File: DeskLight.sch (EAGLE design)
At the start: 39 parts, among them IC1 REG1117, J1 Würth Elektronik SD Connector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, T1 MMBT2222, T2 MMBT2222, T3 MJD122, T4 MJD122, T5 MJD122, U1 ESP32-WROOM-32D, U2 CH340C

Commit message: .
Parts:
- IC1: device burr-brown:REG1117 -> burr-brown_:REG1117
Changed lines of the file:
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@@
 </classes>
 <parts>
-<part name="J1" library="693071030811_Eagle_WR-CRD_rev20b" deviceset="693071020811" device="" package3d_urn="urn:adsk.eagle:package:16444883/2" value="Würth Elektronik SD Connector 693071020811"/>
-<part name="IC1" library="burr-brown" library_urn="urn:adsk.eagle:library:111" deviceset="REG1117" device="" package3d_urn="urn:adsk.eagle:package:4940/1"/>
+<part name="J1" library="693071030811_Eagle_WR-CRD_rev20b" deviceset="693071020811" device="" package3d_urn="urn:adsk.eagle:package:16444883/2" override_package3d_urn="urn:adsk.eagle:package:21154478/3" override_package_urn="urn:adsk.eagle:footprint:16444854/1" value="Würth Elektronik SD Connector 693071020811"/>
+<part name="IC1" library="burr-brown_" deviceset="REG1117" device="" package3d_urn="urn:adsk.eagle:package:21174474/2"/>
 <part name="C1" library="rcl" library_urn="urn:adsk.eagle:library:334" deviceset="CPOL-EU" device="CT3216" package3d_urn="urn:adsk.eagle:package:23327/2" value="22uF"/>
 <part name="GND1" library="supply1" library_urn="urn:adsk.eagle:library:371" deviceset="GND" device=""/>
@@
 <part name="R3" library="rcl" library_urn="urn:adsk.eagle:library:334" deviceset="R-US_" device="R0603" package3d_urn="urn:adsk.eagle:package:23555/3" value="10k"/>
 <part name="GND2" library="supply1" library_urn="urn:adsk.eagle:library:371" deviceset="GND" device=""/>
-<part name="U1" library="ESP32-WROOM-32D" deviceset="ESP32-WROOM-32D" device=""/>
+<part name="U1" library="ESP32-WROOM-32D" library_urn="urn:adsk.eagle:library:21173998" deviceset="ESP32-WROOM-32D" device="" package3d_urn="urn:adsk.eagle:package:21174001/2"/>
 <part name="T1" library="transistor" library_urn="urn:adsk.eagle:library:402" deviceset="*-NPN-" device="SOT23-BEC" package3d_urn="urn:adsk.eagle:package:28748/2" technology="MMBT2222ALT1" value="MMBT2222"/>
 <part name="T2" library="transistor" library_urn="urn:adsk.eagle:library:402" deviceset="*-NPN-" device="SOT23-BEC" package3d_urn="urn:adsk.eagle:package:28748/2" technology="MMBT2222ALT1" value="MMBT2222"/>
@@
 <part name="C3" library="rcl" library_urn="urn:adsk.eagle:library:334" deviceset="C-EU" device="C0603K" package3d_urn="urn:adsk.eagle:package:23680/2" value="1uF"/>
 <part name="GND3" library="supply1" library_urn="urn:adsk.eagle:library:371" deviceset="GND" device=""/>
-<part name="RESET" library="adafruit" library_urn="urn:adsk.eagle:library:420" deviceset="SPST_TACT" device="-KMR2" package3d_urn="urn:adsk.eagle:package:6240885/1" value="KMR2"/>
+<part name="RESET" library="adafruit" library_urn="urn:adsk.eagle:library:21174610" deviceset="SPST_TACT" device="-KMR2" package3d_urn="urn:adsk.eagle:package:21174604/2" override_package3d_urn="urn:adsk.eagle:package:21154607/4" override_package_urn="urn:adsk.eagle:footprint:6240242/1" value="KMR2"/>
 <part name="GND4" library="supply1" library_urn="urn:adsk.eagle:library:371" deviceset="GND" device=""/>
-<part name="BOOT" library="adafruit" library_urn="urn:adsk.eagle:library:420" deviceset="SPST_TACT" device="-KMR2" package3d_urn="urn:adsk.eagle:package:6240885/1" value="KMR2"/>
+<part name="BOOT" library="adafruit" library_urn="urn:adsk.eagle:library:21174610" deviceset="SPST_TACT" device="-KMR2" package3d_urn="urn:adsk.eagle:package:21174604/2" override_package3d_urn="urn:adsk.eagle:package:21174067/2" override_package_urn="urn:adsk.eagle:footprint:6240242/1" value="KMR2"/>
 <part name="GND16" library="supply1" library_urn="urn:adsk.eagle:library:371" deviceset="GND" device=""/>
 <part name="+3V2" library="supply1" library_urn="urn:adsk.eagle:library:371" deviceset="+3V3" device=""/>
 <part name="GND5" library="supply1" library_urn="urn:adsk.eagle:library:371" deviceset="GND" device=""/>
-<part name="U2" library="SparkFun-IC-Comms" deviceset="CH340C" device=""/>
+<part name="U2" library="SparkFun-IC-Comms" library_urn="urn:adsk.eagle:library:21174484" deviceset="CH340C" device="" package3d_urn="urn:adsk.eagle:package:21174539/2"/>
 <part name="RX" library="led" library_urn="urn:adsk.eagle:library:259" deviceset="LED" device="CHIP-LED0603" package3d_urn="urn:adsk.eagle:package:15819/3" value="BLUE"/>
 <part name="TX" library="led" library_urn="urn:adsk.eagle:library:259" deviceset="LED" device="CHIP-LED0603" package3d_urn="urn:adsk.eagle:package:15819/3" value="RED"/>
@@
 <part name="C5" library="rcl" library_urn="urn:adsk.eagle:library:334" deviceset="C-EU" device="C0603K" package3d_urn="urn:adsk.eagle:package:23680/2" value="0.1uF"/>
 <part name="GND11" library="supply1" library_urn="urn:adsk.eagle:library:371" deviceset="GND" device=""/>
-<part name="USB" library="con-molex-usb" deviceset="MICRO-USB-RECEPTACLE" device="47589-0001" value="MICRO-USB-47589-0001"/>
+<part name="USB" library="con-molex-usb" library_urn="urn:adsk.eagle:library:21174025" deviceset="MICRO-USB-RECEPTACLE" device="47589-0001" package3d_urn="urn:adsk.eagle:package:21174028/2" value="MICRO-USB-47589-0001"/>
 <part name="C4" library="rcl" library_urn="urn:adsk.eagle:library:334" deviceset="C-EU" device="C0603K" package3d_urn="urn:adsk.eagle:package:23680/2" value="0.1uF"/>
 <part name="GND6" library="supply1" library_urn="urn:adsk.eagle:library:371" deviceset="GND" device=""/>
@@
 <part name="GND15" library="supply1" library_urn="urn:adsk.eagle:library:371" deviceset="GND" device=""/>
 <part name="+3V11" library="supply1" library_urn="urn:adsk.eagle:library:371" deviceset="+3V3" device=""/>
-<part name="+12V" library="wirepad" library_urn="urn:adsk.eagle:library:412" deviceset="WIREPAD" device="SMD5-1,8" package3d_urn="urn:adsk.eagle:package:30844/1" value="LEDPAD"/>
-<part name="GREEN" library="wirepad" library_urn="urn:adsk.eagle:library:412" deviceset="WIREPAD" device="SMD5-1,8" package3d_urn="urn:adsk.eagle:package:30844/1" value="LEDPAD"/>
-<part name="RED" library="wirepad" library_urn="urn:adsk.eagle:library:412" deviceset="WIREPAD" device="SMD5-1,8" package3d_urn="urn:adsk.eagle:package:30844/1" value="LEDPAP"/>
-<part name="BLUE" library="wirepad" library_urn="urn:adsk.eagle:library:412" deviceset="WIREPAD" device="SMD5-1,8" package3d_urn="urn:adsk.eagle:package:30844/1" value="LEDPAD"/>
-<part name="VIN" library="wirepad" library_urn="urn:adsk.eagle:library:412" deviceset="WIREPAD" device="SMD5-1,8" package3d_urn="urn:adsk.eagle:package:30844/1" value="LEDPAD"/>
-<part name="GND" library="wirepad" library_urn="urn:adsk.eagle:library:412" deviceset="WIREPAD" device="SMD5-1,8" package3d_urn="urn:adsk.eagle:package:30844/1" value="LEDPAD"/>
-<part name="T3" library="transistor-neu-to92" library_urn="urn:adsk.eagle:library:397" deviceset="MJD31*" device="" package3d_urn="urn:adsk.eagle:package:28765/2" value="MJD122"/>
-<part name="T4" library="transistor-neu-to92" library_urn="urn:adsk.eagle:library:397" deviceset="MJD31*" device="" package3d_urn="urn:adsk.eagle:package:28765/2" value="MJD122"/>
-<part name="T5" library="transistor-neu-to92" library_urn="urn:adsk.eagle:library:397" deviceset="MJD31*" device="" package3d_urn="urn:adsk.eagle:package:28765/2" value="MJD122"/>
+<part name="+12V" library="wirepad" library_urn="urn:adsk.eagle:library:21175076" deviceset="WIREPAD" device="SMD5-1,8" package3d_urn="urn:adsk.eagle:package:21175074/2" value="LEDPAD"/>
+<part name="GREEN" library="wirepad" library_urn="urn:adsk.eagle:library:21175076" deviceset="WIREPAD" device="SMD5-1,8" package3d_urn="urn:adsk.eagle:package:21175074/2" value="LEDPAD"/>
+<part name="RED" library="wirepad" library_urn="urn:adsk.eagle:library:21175076" deviceset="WIREPAD" device="SMD5-1,8" package3d_urn="urn:adsk.eagle:package:21175074/2" value="LEDPAP"/>
+<part name="BLUE" library="wirepad" library_urn="urn:adsk.eagle:library:21175076" deviceset="WIREPAD" device="SMD5-1,8" package3d_urn="urn:adsk.eagle:package:21175074/2" value="LEDPAD"/>
+<part name="VIN" library="wirepad" library_urn="urn:adsk.eagle:library:21175076" deviceset="WIREPAD" device="SMD5-1,8" package3d_urn="urn:adsk.eagle:package:21175074/2" value="LEDPAD"/>
+<part name="GND" library="wirepad" library_urn="urn:adsk.eagle:library:21175076" deviceset="WIREPAD" device="SMD5-1,8" package3d_urn="urn:adsk.eagle:package:21175074/2" value="LEDPAD"/>
+<part name="T3" library="transistor-neu-to92" library_urn="urn:adsk.eagle:library:397" deviceset="MJD31*" device="" package3d_urn="urn:adsk.eagle:package:28765/2" override_package3d_urn="urn:adsk.eagle:package:21154560/2" override_package_urn="urn:adsk.eagle:footprint:28703/1" value="MJD122"/>
+<part name="T4" library="transistor-neu-to92" library_urn="urn:adsk.eagle:library:397" deviceset="MJD31*" device="" package3d_urn="urn:adsk.eagle:package:28765/2" override_package3d_urn="urn:adsk.eagle:package:21154548/2" override_package_urn="urn:adsk.eagle:footprint:28703/1" value="MJD122"/>
+<part name="T5" library="transistor-neu-to92" library_urn="urn:adsk.eagle:library:397" deviceset="MJD31*" device="" package3d_urn="urn:adsk.eagle:package:28765/2" override_package3d_urn="urn:adsk.eagle:package:21154542/2" override_package_urn="urn:adsk.eagle:footprint:28703/1" value="MJD122"/>
 <part name="+3V12" library="supply1" library_urn="urn:adsk.eagle:library:371" deviceset="+3V3" device=""/>
 <part name="R11" library="rcl" library_urn="urn:adsk.eagle:library:334" deviceset="R-US_" device="R0603" package3d_urn="urn:adsk.eagle:package:23555/3" value="1k"/>
@@
 packages will not be understood (or retained) with this version.
 </note>
+<note version="9.4" severity="warning">
+Since Version 9.4, EAGLE supports the overriding of 3D packages
+in schematics and board files. Those overridden 3d packages
+will not be understood (or retained) with this version.
+</note>
 <note version="8.4" severity="warning">

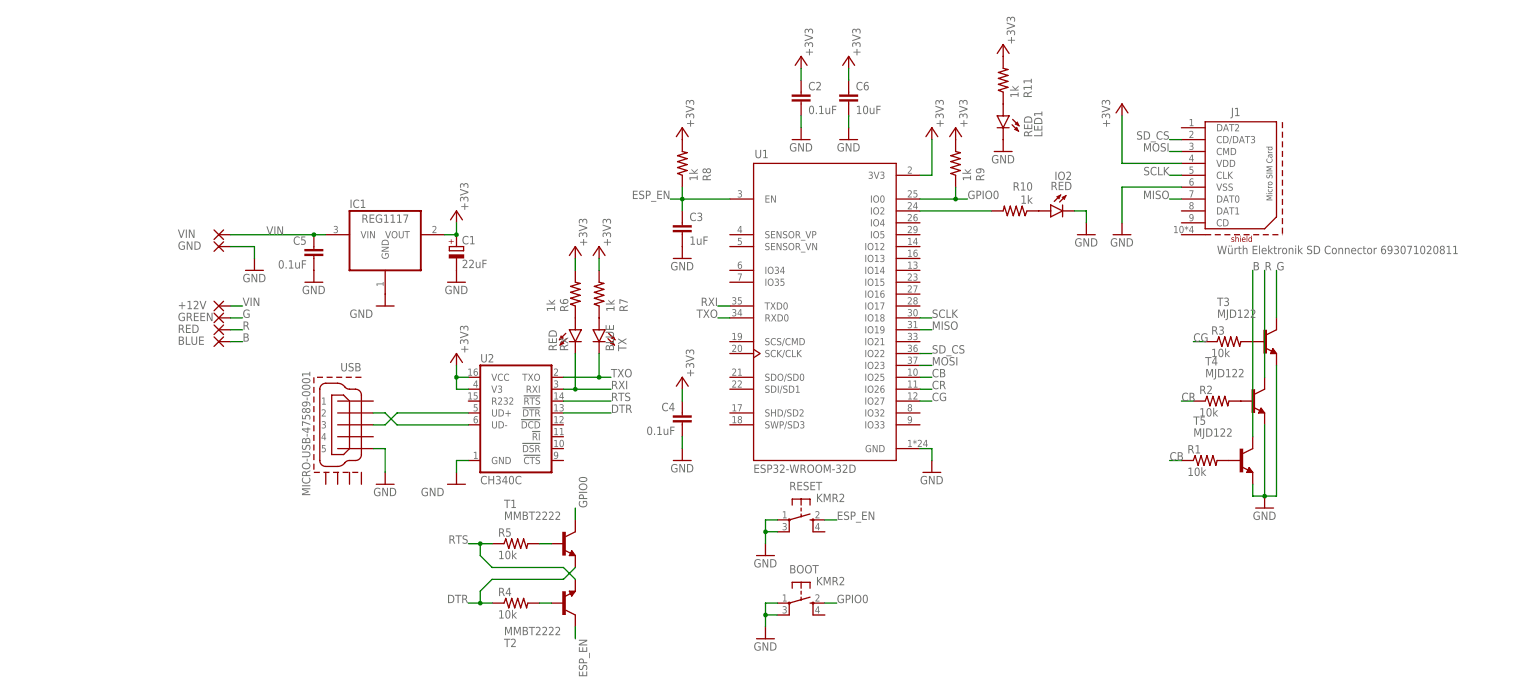
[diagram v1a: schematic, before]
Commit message: new version with small size and for addressable led strips
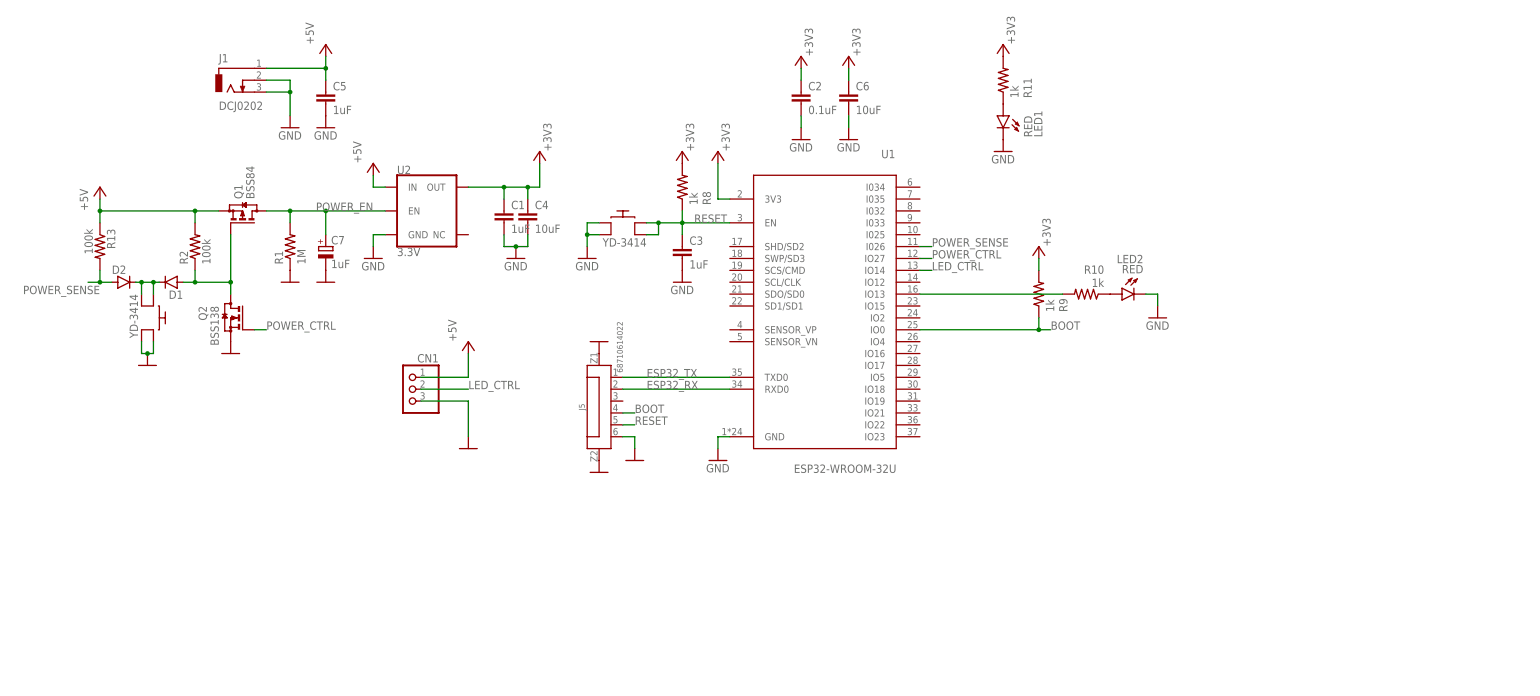
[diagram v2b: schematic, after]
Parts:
- removed +12V, BLUE, GND, GREEN, VIN: LEDPAD, wirepad:WIREPADSMD5-1,8
- removed BOOT, RESET: KMR2, adafruit:SPST_TACT-KMR2
- removed IC1: REG1117, burr-brown_:REG1117
- removed IO2, TX: RED, led:LEDCHIP-LED0603
- removed R3, R4, R5: 10k, rcl:R-US_R0603
- removed R6, R7: 1k, rcl:R-US_R0603
- removed RED: LEDPAP, wirepad:WIREPADSMD5-1,8
- removed RX: BLUE, led:LEDCHIP-LED0603
- removed T1, T2: MMBT2222, transistor:MMBT2222ALT1-NPN-SOT23-BEC
- removed T3, T4, T5: MJD122, transistor-neu-to92:MJD31
- removed USB: MICRO-USB-47589-0001, con-molex-usb:MICRO-USB-RECEPTACLE47589-0001
- added C7: 1uF, rcl:CPOL-EUCT3216
- added CN1: (no value), adafruit:JST_3PIN
- added D1, D2: (no value), semicon-smd-ipc:D-SOD123
- added J5: 68710614022, WR-FPC:6871XX14022_68710614022
- added LED2: RED, led:LEDMICRO-SIDELED
- added Q1: BSS84, transistor-small-signal:BSS84
- added Q2: BSS138, transistor-small-signal:BSS123
- added R13: 100k, rcl:R-US_R0603
- added U$1, U$67: YD-3414, YD-3414:YD-3414
- C1: value 22uF -> 1uF; device rcl:CPOL-EUCT3216 -> rcl:C-EUC0603K
- C4: value 0.1uF -> 10uF; device rcl:C-EUC0603K -> rcl:C-EUC0805
- C5: value 0.1uF -> 1uF
- C6: device rcl:C-EUC0603K -> rcl:C-EUC0805
- J1: value Würth Elektronik SD Connector 693071020811 -> DCJ0202; device 693071030811_Eagle_WR-CRD_rev20b:693071020811 -> con-jack:DCJ0202
- LED1: device led:LEDCHIP-LED0603 -> led:LEDMICRO-SIDELED
- R1: value 10k -> 1M
- R2: value 10k -> 100k
- U1: value ESP32-WROOM-32D -> ESP32-WROOM-32U; device ESP32-WROOM-32D:ESP32-WROOM-32D -> ESP32-WROOM-32U:ESP32-WROOM-32U
- U2: value CH340C -> 3.3V; device SparkFun-IC-Comms:CH340C -> SparkFun-IC-Power:V_REG_AP2112K-3.3V
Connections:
- removed net B: BLUE.P, T5.C
- removed net CB: R1.1, U1.IO25
- removed net CG: R3.1, U1.IO27
- removed net CR: R2.1, U1.IO26
- removed net DTR: R4.1, T1.E, U2.!DTR
- removed net ESP_EN: C3.1, R8.1, RESET.S, T2.C, U1.EN
- removed net G: GREEN.P, T3.C
- removed net GPIO0: BOOT.S, R9.1, T1.C, U1.IO0
- removed net MISO: J1.DAT0, U1.IO19
- removed net MOSI: J1.CMD, U1.IO23
- removed net N$10: R10.2, U1.IO2
- removed net N$12: U2.UD-, USB.2
- removed net N$3: R5.2, T1.B
- removed net N$4: R4.2, T2.B
- removed net N$5: R6.1, RX.A
- removed net N$6: R7.1, TX.A
- removed net N$7: R3.2, T3.B
- removed net R: RED.P, T4.C
- removed net RTS: R5.1, T2.E, U2.!RTS
- removed net RXI: RX.C, U1.TXD0, U2.RXI
- removed net SCLK: J1.CLK, U1.IO18
- removed net SD_CS: J1.CD/DAT3, U1.IO22
- removed net TXO: TX.C, U1.RXD0, U2.TXO
- removed net VIN: +12V.P, C5.1, IC1.VIN, VIN.P
- new net +5V: C5.1, CN1.1, J1.1, Q1.S, R13.1, R2.2, U2.IN
- new net BOOT: J5.4, R9.1, U1.IO0
- new net ESP32_RX: J5.2, U1.RXD0
- new net ESP32_TX: J5.1, U1.TXD0
- new net LED_CTRL: CN1.2, U1.IO14
- new net POWER_CTRL: Q2.G, U1.IO27
- new net POWER_EN: C7.+, Q1.D, R1.2, U2.EN
- new net POWER_SENSE: D2.A, R13.2, U1.I026
- new net RESET: C3.1, J5.5, R8.1, U$1.P$1, U$1.P$2, U1.EN
- net +3V3: now also C1.1, U2.OUT; no longer C1.+, IC1.VOUT, J1.VDD, R6.2, R7.2, U2.V3, U2.VCC
- net GND: now also C1.2, C7.-, CN1.3, J1.2, J1.3, J5.6, J5.Z1, J5.Z2, LED2.C, Q2.S, R1.1, U$1.P$3, U$1.P$4, U$67.P$3, U$67.P$4; no longer BOOT.P, BOOT.P1, C1.-, GND.P, IC1.GND, IO2.C, J1.VSS, RESET.P, RESET.P1, T3.E, T4.E, T5.E, USB.5
- net N$1: now also D1.A, Q1.G, Q2.D, R2.1; no longer R1.2, T5.B
- net N$11: now also D1.C, D2.C, U$67.P$1, U$67.P$2; no longer U2.UD+, USB.3
- net N$13: now also LED2.A; no longer IO2.A
- net N$2: now also R10.2, U1.IO13; no longer R2.2, T4.B
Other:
- moved on the sheet: C3, C4, C5, R1, R10, R2, R8, R9

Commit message: reviewed
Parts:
- C1, C2, C3, C5: device rcl:C-EUC0603K -> rcl:C-EUC0603
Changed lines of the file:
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@@
 <?xml version="1.0" encoding="utf-8"?>
 <!DOCTYPE eagle SYSTEM "eagle.dtd">
-<eagle version="9.6.2">
+<eagle version="9.4.0">
 <drawing>
 <settings>
-<setting alwaysvectorfont="yes"/>
+<setting alwaysvectorfont="no"/>
 <setting verticaltext="up"/>
 </settings>
@@
 <parts>
 <part name="GND2" library="supply1" library_urn="urn:adsk.eagle:library:371" deviceset="GND" device=""/>
-<part name="U1" library="ESP32-WROOM-32U" deviceset="ESP32-WROOM-32U" device="" override_package3d_urn="urn:adsk.eagle:package:27501419/2" override_package_urn="urn:adsk.eagle:footprint:27501420/1"/>
-<part name="C3" library="rcl" library_urn="urn:adsk.eagle:library:334" deviceset="C-EU" device="C0603K" package3d_urn="urn:adsk.eagle:package:23680/2" value="1uF"/>
+<part name="U1" library="ESP32-WROOM-32U" deviceset="ESP32-WROOM-32U" device="" override_package3d_urn="urn:adsk.eagle:package:27501419/2" override_package_urn="urn:adsk.eagle:footprint:27501420/1" override_locally_modified="yes"/>
+<part name="C3" library="rcl" library_urn="urn:adsk.eagle:library:334" deviceset="C-EU" device="C0603" package3d_urn="urn:adsk.eagle:package:23616/2" value="1uF"/>
 <part name="GND3" library="supply1" library_urn="urn:adsk.eagle:library:371" deviceset="GND" device=""/>
 <part name="GND4" library="supply1" library_urn="urn:adsk.eagle:library:371" deviceset="GND" device=""/>
@@
 <part name="+3V7" library="supply1" library_urn="urn:adsk.eagle:library:371" deviceset="+3V3" device=""/>
 <part name="+3V1" library="supply1" library_urn="urn:adsk.eagle:library:371" deviceset="+3V3" device=""/>
-<part name="C2" library="rcl" library_urn="urn:adsk.eagle:library:334" deviceset="C-EU" device="C0603K" package3d_urn="urn:adsk.eagle:package:23680/2" value="0.1uF"/>
+<part name="C2" library="rcl" library_urn="urn:adsk.eagle:library:334" deviceset="C-EU" device="C0603" package3d_urn="urn:adsk.eagle:package:23616/2" value="0.1uF"/>
 <part name="C6" library="rcl" library_urn="urn:adsk.eagle:library:334" deviceset="C-EU" device="C0805" package3d_urn="urn:adsk.eagle:package:23617/2" value="10uF"/>
 <part name="+3V8" library="supply1" library_urn="urn:adsk.eagle:library:371" deviceset="+3V3" device=""/>
@@
 <part name="GND17" library="supply1" library_urn="urn:adsk.eagle:library:371" deviceset="GND" device=""/>
 <part name="U2" library="SparkFun-IC-Power" library_urn="urn:adsk.eagle:library:526" deviceset="V_REG_AP2112" device="K-3.3V" package3d_urn="urn:adsk.eagle:package:39060/1" override_package3d_urn="urn:adsk.eagle:package:27501300/2" override_package_urn="urn:adsk.eagle:footprint:39006/1" value="3.3V"/>
-<part name="C1" library="rcl" library_urn="urn:adsk.eagle:library:334" deviceset="C-EU" device="C0603K" package3d_urn="urn:adsk.eagle:package:23680/2" value="1uF"/>
+<part name="C1" library="rcl" library_urn="urn:adsk.eagle:library:334" deviceset="C-EU" device="C0603" package3d_urn="urn:adsk.eagle:package:23616/2" value="1uF"/>
 <part name="C4" library="rcl" library_urn="urn:adsk.eagle:library:334" deviceset="C-EU" device="C0805" package3d_urn="urn:adsk.eagle:package:23617/2" value="10uF"/>
 <part name="GND5" library="supply1" library_urn="urn:adsk.eagle:library:371" deviceset="GND" device=""/>
-<part name="C5" library="rcl" library_urn="urn:adsk.eagle:library:334" deviceset="C-EU" device="C0603K" package3d_urn="urn:adsk.eagle:package:23680/2" value="1uF"/>
+<part name="C5" library="rcl" library_urn="urn:adsk.eagle:library:334" deviceset="C-EU" device="C0603" package3d_urn="urn:adsk.eagle:package:23616/2" value="1uF"/>
 <part name="GND6" library="supply1" library_urn="urn:adsk.eagle:library:371" deviceset="GND" device=""/>
 <part name="GND1" library="supply1" library_urn="urn:adsk.eagle:library:371" deviceset="GND" device=""/>
